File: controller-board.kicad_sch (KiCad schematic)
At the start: 49 parts, among them J1 J_CM5, J2 J_IR, J3 J_SWD, J4 J_SAFE, J5 J_LED, J6 J_STACK, Q1 2N7002, Q2 2N7002, Q3 SI2301CDS, SW1 SW_Push, U1 AMS1117-3.3, U2 STM32G474RETx, Y1 8MHz, Y2 32.768kHz

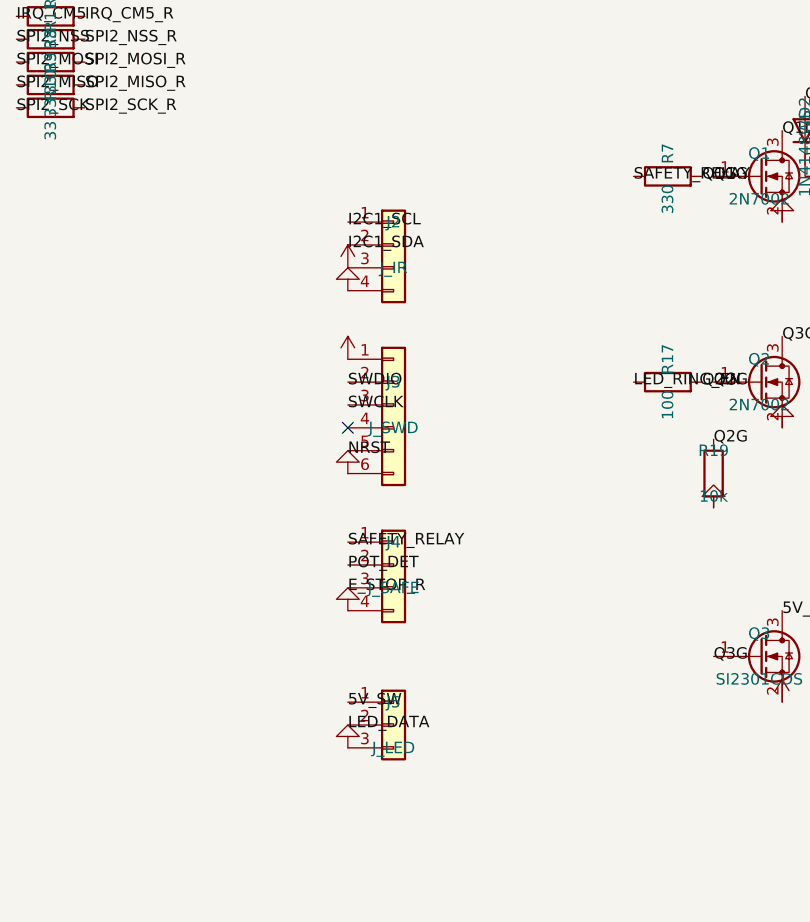
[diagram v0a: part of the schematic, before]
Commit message: refactor(hw): merge J_IR and J_LED into single J_IR_LED Hirose DF11-8DP-2DS connector
Replace two separate connectors (J_IR 4-pin JST-SH + J_LED 3-pin JST-XH) with a
single J_IR_LED 2x4 Hirose DF11-8DP-2DS dual-row connector, reducing connector
count from 17 to 16. Pins 1-4 carry IR sensor I2C + power, pins 5-8 carry LED
ring switched 5V + data + GND + spare.

Co-Authored-By: Claude Opus 4.6 <noreply@anthropic.com>
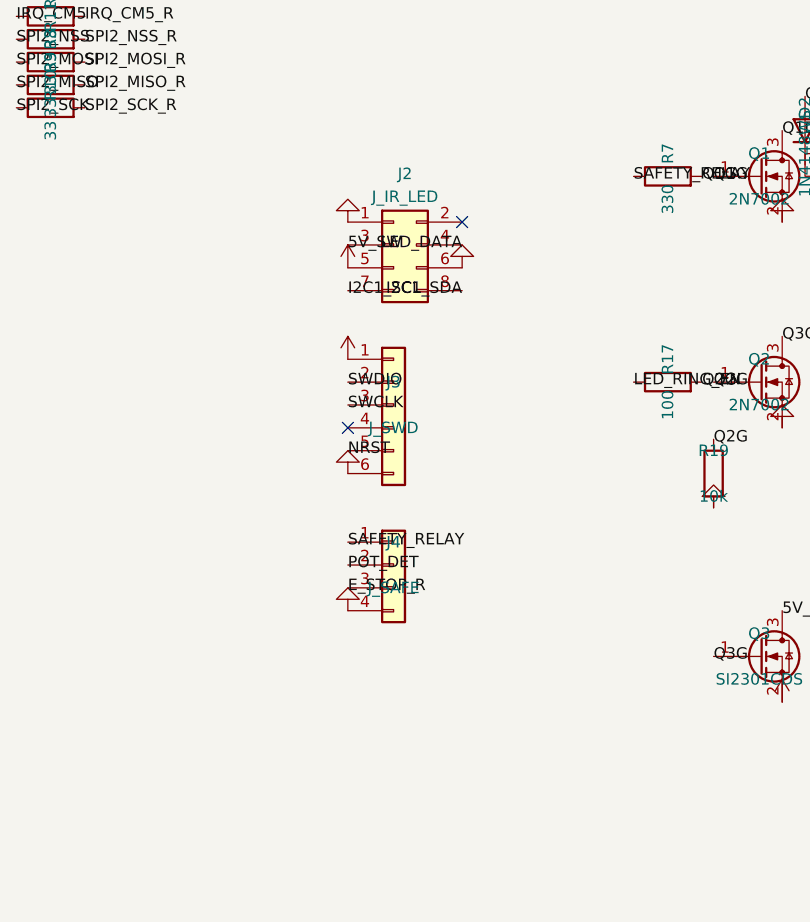
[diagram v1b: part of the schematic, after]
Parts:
- removed J5: J_LED, Connector_JST:JST_XH_B3B-XH-A_1x03_P2.50mm_Vertical, symbol Connector_Generic:Conn_01x03
- J2: value J_IR -> J_IR_LED; footprint Connector_JST:JST_SH_SM04B-SRSS-TB_1x04-1MP_P1.00mm_Horizontal -> Connector_Hirose:Hirose_DF11-8DP-2DSA_2x04_P2.00mm_Vertical; symbol Connector_Generic:Conn_01x04 -> Connector_Generic:Conn_02x04_Odd_Even
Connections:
- net +3V3: now also J2.5 (Pin_5); no longer J2.3 (Pin_3)
- net 5V_SW: now also J2.3 (Pin_3)
- net GND: now also J2.1 (Pin_1), J2.6 (Pin_6); no longer J2.4 (Pin_4)
- net I2C1_SCL: now also J2.7 (Pin_7); no longer J2.1 (Pin_1)
- net I2C1_SDA: now also J2.8 (Pin_8); no longer J2.2 (Pin_2)
- net LED_DATA: now also J2.4 (Pin_4)
- no-connect marks 37 -> 38
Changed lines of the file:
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@@
 	)
 	(symbol
-		(lib_id "Connector_Generic:Conn_01x04")
-		(at 208.28 182.88 0)
-		(unit 1)
-		(exclude_from_sim no) (in_bom yes) (on_board yes) (dnp no)
-		(property "Reference" "J2" (at 208.28 180.34 0) (effects (font (size 1.27 1.27))))
-		(property "Value" "J_IR" (at 208.28 185.42 0) (effects (font (size 1.27 1.27))))
-		(property "Footprint" "Connector_JST:JST_SH_SM04B-SRSS-TB_1x04-1MP_P1.00mm_Horizontal" (at 208.28 182.88 0) (effects (font (size 1.27 1.27)) (hide yes)))
-		(property "Datasheet" "~" (at 208.28 182.88 0) (effects (font (size 1.27 1.27)) (hide yes)))
+		(lib_id "Connector_Generic:Conn_02x04_Odd_Even")
+		(at 208.28 184.15 0)
+		(unit 1)
+		(exclude_from_sim no) (in_bom yes) (on_board yes) (dnp no)
+		(property "Reference" "J2" (at 209.55 174.9762 0) (effects (font (size 1.27 1.27))))
+		(property "Value" "J_IR_LED" (at 209.55 177.5162 0) (effects (font (size 1.27 1.27))))
+		(property "Footprint" "Connector_Hirose:Hirose_DF11-8DP-2DSA_2x04_P2.00mm_Vertical" (at 208.28 184.15 0) (effects (font (size 1.27 1.27)) (hide yes)))
+		(property "Datasheet" "~" (at 208.28 184.15 0) (effects (font (size 1.27 1.27)) (hide yes)))
 		(pin "1")
 		(pin "2")
 		(pin "3")
 		(pin "4")
+		(pin "5")
+		(pin "6")
+		(pin "7")
+		(pin "8")
 		(instances (project "controller-board" (path "/1f983e30-f107-4597-a85a-d2daa79ab050" (reference "J2") (unit 1))))
 	)
@@
 		(pin "4")
 		(instances (project "controller-board" (path "/1f983e30-f107-4597-a85a-d2daa79ab050" (reference "J4") (unit 1))))
-	)
-	(symbol
-		(lib_id "Connector_Generic:Conn_01x03")
-		(at 208.28 236.22 0)
-		(unit 1)
-		(exclude_from_sim no) (in_bom yes) (on_board yes) (dnp no)
-		(property "Reference" "J5" (at 208.28 233.68 0) (effects (font (size 1.27 1.27))))
-		(property "Value" "J_LED" (at 208.28 238.76 0) (effects (font (size 1.27 1.27))))
-		(property "Footprint" "Connector_JST:JST_XH_B3B-XH-A_1x03_P2.50mm_Vertical" (at 208.28 236.22 0) (effects (font (size 1.27 1.27)) (hide yes)))
-		(property "Datasheet" "~" (at 208.28 236.22 0) (effects (font (size 1.27 1.27)) (hide yes)))
-		(pin "1")
-		(pin "2")
-		(pin "3")
-		(instances (project "controller-board" (path "/1f983e30-f107-4597-a85a-d2daa79ab050" (reference "J5") (unit 1))))
 	)
 	(symbol
@@
 	)
 	(symbol
-		(lib_id "power:GND") (at 203.2 187.96 180) (unit 1)
-		(exclude_from_sim no) (in_bom no) (on_board yes) (dnp no)
-		(property "Reference" "#PWR0054" (at 203.2 185.42000000000002 0) (effects (font (size 1.27 1.27)) (hide yes)))
-		(property "Value" "GND" (at 203.2 190.5 0) (effects (font (size 1.27 1.27)) (hide yes)))
+		(lib_id "power:GND") (at 215.9 185.42 180) (unit 1)
+		(exclude_from_sim no) (in_bom no) (on_board yes) (dnp no)
+		(property "Reference" "#PWR0054" (at 215.9 182.88 0) (effects (font (size 1.27 1.27)) (hide yes)))
+		(property "Value" "GND" (at 215.9 187.96 0) (effects (font (size 1.27 1.27)) (hide yes)))
 		(pin "1")
 		(instances (project "controller-board" (path "/1f983e30-f107-4597-a85a-d2daa79ab050" (reference "#PWR0054") (unit 1))))
@@
 	)
 	(symbol
-		(lib_id "power:GND") (at 203.2 238.76 180) (unit 1)
-		(exclude_from_sim no) (in_bom no) (on_board yes) (dnp no)
-		(property "Reference" "#PWR0058" (at 203.2 236.22 0) (effects (font (size 1.27 1.27)) (hide yes)))
-		(property "Value" "GND" (at 203.2 241.29999999999998 0) (effects (font (size 1.27 1.27)) (hide yes)))
+		(lib_id "power:GND") (at 203.2 180.34 180) (unit 1)
+		(exclude_from_sim no) (in_bom no) (on_board yes) (dnp no)
+		(property "Reference" "#PWR0058" (at 203.2 177.8 0) (effects (font (size 1.27 1.27)) (hide yes)))
+		(property "Value" "GND" (at 203.2 182.88 0) (effects (font (size 1.27 1.27)) (hide yes)))
 		(pin "1")
 		(instances (project "controller-board" (path "/1f983e30-f107-4597-a85a-d2daa79ab050" (reference "#PWR0058") (unit 1))))
@@
 	(label "SPI2_SCK_R" (at 203.2 132.08 0) (effects (font (size 1.27 1.27))))
 	(label "SPI2_NSS_R" (at 215.9 132.08 0) (effects (font (size 1.27 1.27))))
-	(label "I2C1_SCL" (at 203.2 180.34 0) (effects (font (size 1.27 1.27))))
-	(label "I2C1_SDA" (at 203.2 182.88 0) (effects (font (size 1.27 1.27))))
+	(label "I2C1_SCL" (at 203.2 187.96 0) (effects (font (size 1.27 1.27))))
+	(label "I2C1_SDA" (at 215.9 187.96 180) (effects (font (size 1.27 1.27))))
 	(label "SWDIO" (at 203.2 198.12 0) (effects (font (size 1.27 1.27))))
 	(label "SWCLK" (at 203.2 200.66 0) (effects (font (size 1.27 1.27))))
@@
 	(label "POT_DET" (at 203.2 218.44 0) (effects (font (size 1.27 1.27))))
 	(label "E_STOP_R" (at 203.2 220.98 0) (effects (font (size 1.27 1.27))))
-	(label "5V_SW" (at 203.2 233.68 0) (effects (font (size 1.27 1.27))))
-	(label "LED_DATA" (at 203.2 236.22 0) (effects (font (size 1.27 1.27))))
+	(label "5V_SW" (at 203.2 182.88 0) (effects (font (size 1.27 1.27))))
+	(label "LED_DATA" (at 215.9 182.88 180) (effects (font (size 1.27 1.27))))
 	(label "PASD_PUMP_PWM" (at 121.92 254.0 0) (effects (font (size 1.27 1.27))))
 	(label "HX711_SCK" (at 121.92 256.54 0) (effects (font (size 1.27 1.27))))
@@
 	(no_connect (at 215.9 152.4))
 	(no_connect (at 203.2 203.2))
+	(no_connect (at 215.9 180.34))
 	(symbol
 		(lib_id "power:PWR_FLAG") (at 134.62 78.74 0) (unit 1)
